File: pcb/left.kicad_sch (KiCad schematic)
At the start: 112 parts, among them J1 PJ-320A, SW1 =, SW10 E, SW11 R, SW12 T, SW13 Esc, SW14 A, SW15 S, SW16 D, SW17 F, SW18 G, SW19 Alt, SW2 1, SW20 Shift, SW21 Z, SW22 X, SW23 C, SW24 V, SW25 B, SW26 Ctrl, SW27 `, SW28 Caps, SW29 Left, SW3 2, SW30 Right, SW31 Super, SW32 Bksp, SW33 Del, SW4 3, SW5 4, SW6 5, SW7 Tab, SW8 Q, SW9 W, SW90 MSK12C02 power, SW91 Reset, U1 nRF52840 Pro Micro

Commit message: Merge both halves into one KiCad project
pcb/keygen.kicad_pro holds a top sheet with left and right sub-sheets
(refs 1xx/2xx, sheet-local nets) and will carry one PCB with both halves
joined by snap-off tabs. The board stays non-reversible. The checker now
runs ERC on the whole project and splits the netlist per half.
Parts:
- removed BT1: LiPo 3.7V ~1000mAh, Connector_JST:JST_PH_S2B-PH-K_1x02_P2.00mm_Horizontal, symbol Device:Battery_Cell
- removed C1: 10uF, Capacitor_SMD:C_0805_2012Metric, symbol Device:C
- removed C2: 100nF, Capacitor_SMD:C_0805_2012Metric, symbol Device:C
- removed D1, D10, D11, D12, D13, D14, D15, D16, D17, D18, D19, D2, D20, D21, D22, D23, D24, D25, D26, D27, D28, D29, D3, D30, D31, D32, D33, D4, D5, D6, D7, D8, D9: 1N4148, Diode_THT:D_DO-35_SOD27_P7.62mm_Horizontal, symbol Device:D
- removed J1: PJ-320A, Keebio-Parts:TRRS-PJ-320A, symbol keygen:TRRS_PJ-320A
- removed LED1, LED10, LED11, LED12, LED13, LED14, LED15, LED16, LED17, LED18, LED19, LED2, LED20, LED21, LED22, LED23, LED24, LED25, LED26, LED27, LED28, LED29, LED3, LED30, LED31, LED32, LED33, LED34, LED35, LED36, LED37, LED38, LED39, LED4, LED5, LED6, LED7, LED8, LED9: SK6812MINI-E, LED_SMD:LED_SK6812MINI-E_3.2x2.8mm_P1.5mm_ReverseMount, symbol LED:SK6812MINI-E
- removed SW1: =, marbastlib-mx:SW_MX_HS_CPG151101S11_1.25u, symbol marbastlib-mx:MX_SW_HS_CPG151101S11
- removed SW10: E, marbastlib-mx:SW_MX_HS_CPG151101S11_1u, symbol marbastlib-mx:MX_SW_HS_CPG151101S11
- removed SW11: R, marbastlib-mx:SW_MX_HS_CPG151101S11_1u, symbol marbastlib-mx:MX_SW_HS_CPG151101S11
- removed SW12: T, marbastlib-mx:SW_MX_HS_CPG151101S11_1u, symbol marbastlib-mx:MX_SW_HS_CPG151101S11
- removed SW13: Esc, marbastlib-mx:SW_MX_HS_CPG151101S11_1.25u, symbol marbastlib-mx:MX_SW_HS_CPG151101S11
- removed SW14: A, marbastlib-mx:SW_MX_HS_CPG151101S11_1u, symbol marbastlib-mx:MX_SW_HS_CPG151101S11
- removed SW15: S, marbastlib-mx:SW_MX_HS_CPG151101S11_1u, symbol marbastlib-mx:MX_SW_HS_CPG151101S11
- removed SW16: D, marbastlib-mx:SW_MX_HS_CPG151101S11_1u, symbol marbastlib-mx:MX_SW_HS_CPG151101S11
- removed SW17: F, marbastlib-mx:SW_MX_HS_CPG151101S11_1u, symbol marbastlib-mx:MX_SW_HS_CPG151101S11
- removed SW18: G, marbastlib-mx:SW_MX_HS_CPG151101S11_1u, symbol marbastlib-mx:MX_SW_HS_CPG151101S11
- removed SW19: Alt, marbastlib-mx:SW_MX_HS_CPG151101S11_1u, symbol marbastlib-mx:MX_SW_HS_CPG151101S11
- removed SW2: 1, marbastlib-mx:SW_MX_HS_CPG151101S11_1u, symbol marbastlib-mx:MX_SW_HS_CPG151101S11
- removed SW20: Shift, marbastlib-mx:SW_MX_HS_CPG151101S11_1.25u, symbol marbastlib-mx:MX_SW_HS_CPG151101S11
- removed SW21: Z, marbastlib-mx:SW_MX_HS_CPG151101S11_1u, symbol marbastlib-mx:MX_SW_HS_CPG151101S11
- removed SW22: X, marbastlib-mx:SW_MX_HS_CPG151101S11_1u, symbol marbastlib-mx:MX_SW_HS_CPG151101S11
- removed SW23: C, marbastlib-mx:SW_MX_HS_CPG151101S11_1u, symbol marbastlib-mx:MX_SW_HS_CPG151101S11
- removed SW24: V, marbastlib-mx:SW_MX_HS_CPG151101S11_1u, symbol marbastlib-mx:MX_SW_HS_CPG151101S11
- removed SW25: B, marbastlib-mx:SW_MX_HS_CPG151101S11_1u, symbol marbastlib-mx:MX_SW_HS_CPG151101S11
- removed SW26: Ctrl, marbastlib-mx:SW_MX_HS_CPG151101S11_1u, symbol marbastlib-mx:MX_SW_HS_CPG151101S11
- removed SW27: `, marbastlib-mx:SW_MX_HS_CPG151101S11_1u, symbol marbastlib-mx:MX_SW_HS_CPG151101S11
- removed SW28: Caps, marbastlib-mx:SW_MX_HS_CPG151101S11_1u, symbol marbastlib-mx:MX_SW_HS_CPG151101S11
- removed SW29: Left, marbastlib-mx:SW_MX_HS_CPG151101S11_1u, symbol marbastlib-mx:MX_SW_HS_CPG151101S11
- removed SW3: 2, marbastlib-mx:SW_MX_HS_CPG151101S11_1u, symbol marbastlib-mx:MX_SW_HS_CPG151101S11
- removed SW30: Right, marbastlib-mx:SW_MX_HS_CPG151101S11_1u, symbol marbastlib-mx:MX_SW_HS_CPG151101S11
- removed SW31: Super, marbastlib-mx:SW_MX_HS_CPG151101S11_1.25u, symbol marbastlib-mx:MX_SW_HS_CPG151101S11
- removed SW32: Bksp, marbastlib-mx:SW_MX_HS_CPG151101S11_1.5u, symbol marbastlib-mx:MX_SW_HS_CPG151101S11
- removed SW33: Del, marbastlib-mx:SW_MX_HS_CPG151101S11_1.5u, symbol marbastlib-mx:MX_SW_HS_CPG151101S11
- removed SW4: 3, marbastlib-mx:SW_MX_HS_CPG151101S11_1u, symbol marbastlib-mx:MX_SW_HS_CPG151101S11
- removed SW5: 4, marbastlib-mx:SW_MX_HS_CPG151101S11_1u, symbol marbastlib-mx:MX_SW_HS_CPG151101S11
- removed SW6: 5, marbastlib-mx:SW_MX_HS_CPG151101S11_1u, symbol marbastlib-mx:MX_SW_HS_CPG151101S11
- removed SW7: Tab, marbastlib-mx:SW_MX_HS_CPG151101S11_1.25u, symbol marbastlib-mx:MX_SW_HS_CPG151101S11
- removed SW8: Q, marbastlib-mx:SW_MX_HS_CPG151101S11_1u, symbol marbastlib-mx:MX_SW_HS_CPG151101S11
- removed SW9: W, marbastlib-mx:SW_MX_HS_CPG151101S11_1u, symbol marbastlib-mx:MX_SW_HS_CPG151101S11
- removed SW90: MSK12C02 power, marbastlib-various:SW_MSK12C02-HB, symbol Switch:SW_SPDT
- removed SW91: Reset, Button_Switch_THT:SW_PUSH_6mm_H5mm, symbol Switch:SW_Push
- removed U1: nRF52840 Pro Micro, marbastlib-xp-promicroish:nice_nano_H_USBup, symbol keygen:nice_nano_v2
- added BT101: LiPo 3.7V ~1000mAh, Connector_JST:JST_PH_S2B-PH-K_1x02_P2.00mm_Horizontal, symbol Device:Battery_Cell
- added C101: 10uF, Capacitor_SMD:C_0805_2012Metric, symbol Device:C
- added C102: 100nF, Capacitor_SMD:C_0805_2012Metric, symbol Device:C
- added D101, D102, D103, D104, D105, D106, D107, D108, D109, D110, D111, D112, D113, D114, D115, D116, D117, D118, D119, D120, D121, D122, D123, D124, D125, D126, D127, D128, D129, D130, D131, D132, D133: 1N4148, Diode_THT:D_DO-35_SOD27_P7.62mm_Horizontal, symbol Device:D
- added J101: PJ-320A, Keebio-Parts:TRRS-PJ-320A, symbol keygen:TRRS_PJ-320A
- added LED101, LED102, LED103, LED104, LED105, LED106, LED107, LED108, LED109, LED110, LED111, LED112, LED113, LED114, LED115, LED116, LED117, LED118, LED119, LED120, LED121, LED122, LED123, LED124, LED125, LED126, LED127, LED128, LED129, LED130, LED131, LED132, LED133, LED134, LED135, LED136, LED137, LED138, LED139: SK6812MINI-E, LED_SMD:LED_SK6812MINI-E_3.2x2.8mm_P1.5mm_ReverseMount, symbol LED:SK6812MINI-E
- added SW101: =, marbastlib-mx:SW_MX_HS_CPG151101S11_1.25u, symbol marbastlib-mx:MX_SW_HS_CPG151101S11
- added SW102: 1, marbastlib-mx:SW_MX_HS_CPG151101S11_1u, symbol marbastlib-mx:MX_SW_HS_CPG151101S11
- added SW103: 2, marbastlib-mx:SW_MX_HS_CPG151101S11_1u, symbol marbastlib-mx:MX_SW_HS_CPG151101S11
- added SW104: 3, marbastlib-mx:SW_MX_HS_CPG151101S11_1u, symbol marbastlib-mx:MX_SW_HS_CPG151101S11
- added SW105: 4, marbastlib-mx:SW_MX_HS_CPG151101S11_1u, symbol marbastlib-mx:MX_SW_HS_CPG151101S11
- added SW106: 5, marbastlib-mx:SW_MX_HS_CPG151101S11_1u, symbol marbastlib-mx:MX_SW_HS_CPG151101S11
- added SW107: Tab, marbastlib-mx:SW_MX_HS_CPG151101S11_1.25u, symbol marbastlib-mx:MX_SW_HS_CPG151101S11
- added SW108: Q, marbastlib-mx:SW_MX_HS_CPG151101S11_1u, symbol marbastlib-mx:MX_SW_HS_CPG151101S11
- added SW109: W, marbastlib-mx:SW_MX_HS_CPG151101S11_1u, symbol marbastlib-mx:MX_SW_HS_CPG151101S11
- added SW110: E, marbastlib-mx:SW_MX_HS_CPG151101S11_1u, symbol marbastlib-mx:MX_SW_HS_CPG151101S11
- added SW111: R, marbastlib-mx:SW_MX_HS_CPG151101S11_1u, symbol marbastlib-mx:MX_SW_HS_CPG151101S11
- added SW112: T, marbastlib-mx:SW_MX_HS_CPG151101S11_1u, symbol marbastlib-mx:MX_SW_HS_CPG151101S11
- added SW113: Esc, marbastlib-mx:SW_MX_HS_CPG151101S11_1.25u, symbol marbastlib-mx:MX_SW_HS_CPG151101S11
- added SW114: A, marbastlib-mx:SW_MX_HS_CPG151101S11_1u, symbol marbastlib-mx:MX_SW_HS_CPG151101S11
- added SW115: S, marbastlib-mx:SW_MX_HS_CPG151101S11_1u, symbol marbastlib-mx:MX_SW_HS_CPG151101S11
- added SW116: D, marbastlib-mx:SW_MX_HS_CPG151101S11_1u, symbol marbastlib-mx:MX_SW_HS_CPG151101S11
- added SW117: F, marbastlib-mx:SW_MX_HS_CPG151101S11_1u, symbol marbastlib-mx:MX_SW_HS_CPG151101S11
- added SW118: G, marbastlib-mx:SW_MX_HS_CPG151101S11_1u, symbol marbastlib-mx:MX_SW_HS_CPG151101S11
- added SW119: Alt, marbastlib-mx:SW_MX_HS_CPG151101S11_1u, symbol marbastlib-mx:MX_SW_HS_CPG151101S11
- added SW120: Shift, marbastlib-mx:SW_MX_HS_CPG151101S11_1.25u, symbol marbastlib-mx:MX_SW_HS_CPG151101S11
- added SW121: Z, marbastlib-mx:SW_MX_HS_CPG151101S11_1u, symbol marbastlib-mx:MX_SW_HS_CPG151101S11
- added SW122: X, marbastlib-mx:SW_MX_HS_CPG151101S11_1u, symbol marbastlib-mx:MX_SW_HS_CPG151101S11
- added SW123: C, marbastlib-mx:SW_MX_HS_CPG151101S11_1u, symbol marbastlib-mx:MX_SW_HS_CPG151101S11
- added SW124: V, marbastlib-mx:SW_MX_HS_CPG151101S11_1u, symbol marbastlib-mx:MX_SW_HS_CPG151101S11
- added SW125: B, marbastlib-mx:SW_MX_HS_CPG151101S11_1u, symbol marbastlib-mx:MX_SW_HS_CPG151101S11
- added SW126: Ctrl, marbastlib-mx:SW_MX_HS_CPG151101S11_1u, symbol marbastlib-mx:MX_SW_HS_CPG151101S11
- added SW127: `, marbastlib-mx:SW_MX_HS_CPG151101S11_1u, symbol marbastlib-mx:MX_SW_HS_CPG151101S11
- added SW128: Caps, marbastlib-mx:SW_MX_HS_CPG151101S11_1u, symbol marbastlib-mx:MX_SW_HS_CPG151101S11
- added SW129: Left, marbastlib-mx:SW_MX_HS_CPG151101S11_1u, symbol marbastlib-mx:MX_SW_HS_CPG151101S11
- added SW130: Right, marbastlib-mx:SW_MX_HS_CPG151101S11_1u, symbol marbastlib-mx:MX_SW_HS_CPG151101S11
- added SW131: Super, marbastlib-mx:SW_MX_HS_CPG151101S11_1.25u, symbol marbastlib-mx:MX_SW_HS_CPG151101S11
- added SW132: Bksp, marbastlib-mx:SW_MX_HS_CPG151101S11_1.5u, symbol marbastlib-mx:MX_SW_HS_CPG151101S11
- added SW133: Del, marbastlib-mx:SW_MX_HS_CPG151101S11_1.5u, symbol marbastlib-mx:MX_SW_HS_CPG151101S11
- added SW190: MSK12C02 power, marbastlib-various:SW_MSK12C02-HB, symbol Switch:SW_SPDT
- added SW191: Reset, Button_Switch_THT:SW_PUSH_6mm_H5mm, symbol Switch:SW_Push
- added U101: nRF52840 Pro Micro, marbastlib-xp-promicroish:nice_nano_H_USBup, symbol keygen:nice_nano_v2
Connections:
- net BAT_RAW: now also BT101.1 (+), SW190.1 (A)
- net COL0: now also SW101.1, SW107.1, SW113.1, SW120.1, SW127.1, U101.12 (P1.06)
- net COL1: now also SW102.1, SW108.1, SW114.1, SW121.1, SW128.1, U101.22 (P1.11)
- net COL2: now also SW103.1, SW109.1, SW115.1, SW122.1, SW129.1, U101.21 (P1.13)
- net COL3: now also SW104.1, SW110.1, SW116.1, SW123.1, SW130.1, U101.20 (P1.15)
- net COL4: now also SW105.1, SW111.1, SW117.1, SW124.1, SW131.1, U101.19 (P0.02)
- net COL5: now also SW106.1, SW112.1, SW118.1, SW125.1, SW132.1, U101.18 (P0.29)
- net COL6: now also SW119.1, SW126.1, SW133.1, U101.17 (P0.31)
- net GND: now also BT101.2 (-), C101.2, C102.2, J101.1 (S), LED101.1 (VSS), LED102.1 (VSS), LED103.1 (VSS), LED104.1 (VSS), LED105.1 (VSS), LED106.1 (VSS), LED107.1 (VSS), LED108.1 (VSS), LED109.1 (VSS), LED110.1 (VSS), LED111.1 (VSS), LED112.1 (VSS), LED113.1 (VSS), LED114.1 (VSS), LED115.1 (VSS), LED116.1 (VSS), LED117.1 (VSS), LED118.1 (VSS), LED119.1 (VSS), LED120.1 (VSS), LED121.1 (VSS), LED122.1 (VSS), LED123.1 (VSS), LED124.1 (VSS), LED125.1 (VSS), LED126.1 (VSS), LED127.1 (VSS), LED128.1 (VSS), LED129.1 (VSS), LED130.1 (VSS), LED131.1 (VSS), LED132.1 (VSS), LED133.1 (VSS), LED134.1 (VSS), LED135.1 (VSS), LED136.1 (VSS), LED137.1 (VSS), LED138.1 (VSS), LED139.1 (VSS), SW191.2, U101.14 (GND), U101.3 (GND), U101.4 (GND)
- net K00: now also D101.2 (A), SW101.2
- net K01: now also D102.2 (A), SW102.2
- net K02: now also D103.2 (A), SW103.2
- net K03: now also D104.2 (A), SW104.2
- net K04: now also D105.2 (A), SW105.2
- net K05: now also D106.2 (A), SW106.2
- net K10: now also D107.2 (A), SW107.2
- net K11: now also D108.2 (A), SW108.2
- net K12: now also D109.2 (A), SW109.2
- net K13: now also D110.2 (A), SW110.2
- net K14: now also D111.2 (A), SW111.2
- net K15: now also D112.2 (A), SW112.2
- net K20: now also D113.2 (A), SW113.2
- net K21: now also D114.2 (A), SW114.2
- net K22: now also D115.2 (A), SW115.2
- net K23: now also D116.2 (A), SW116.2
- net K24: now also D117.2 (A), SW117.2
- net K25: now also D118.2 (A), SW118.2
- net K26: now also D119.2 (A), SW119.2
- net K30: now also D120.2 (A), SW120.2
- net K31: now also D121.2 (A), SW121.2
- net K32: now also D122.2 (A), SW122.2
- net K33: now also D123.2 (A), SW123.2
- net K34: now also D124.2 (A), SW124.2
- net K35: now also D125.2 (A), SW125.2
- net K36: now also D126.2 (A), SW126.2
- net K40: now also D127.2 (A), SW127.2
- net K41: now also D128.2 (A), SW128.2
- net K42: now also D129.2 (A), SW129.2
- net K43: now also D130.2 (A), SW130.2
- net K44: now also D131.2 (A), SW131.2
- net K45: now also D132.2 (A), SW132.2
- net K46: now also D133.2 (A), SW133.2
- net LED_D1: now also LED101.4 (DOUT), LED102.2 (DIN)
- net LED_D10: now also LED110.4 (DOUT), LED111.2 (DIN)
- net LED_D11: now also LED111.4 (DOUT), LED112.2 (DIN)
- net LED_D12: now also LED112.4 (DOUT), LED113.2 (DIN)
- net LED_D13: now also LED113.4 (DOUT), LED114.2 (DIN)
- net LED_D14: now also LED114.4 (DOUT), LED115.2 (DIN)
- net LED_D15: now also LED115.4 (DOUT), LED116.2 (DIN)
- net LED_D16: now also LED116.4 (DOUT), LED117.2 (DIN)
- net LED_D17: now also LED117.4 (DOUT), LED118.2 (DIN)
- net LED_D18: now also LED118.4 (DOUT), LED119.2 (DIN)
- net LED_D19: now also LED119.4 (DOUT), LED120.2 (DIN)
- net LED_D2: now also LED102.4 (DOUT), LED103.2 (DIN)
- net LED_D20: now also LED120.4 (DOUT), LED121.2 (DIN)
- net LED_D21: now also LED121.4 (DOUT), LED122.2 (DIN)
- net LED_D22: now also LED122.4 (DOUT), LED123.2 (DIN)
- net LED_D23: now also LED123.4 (DOUT), LED124.2 (DIN)
- net LED_D24: now also LED124.4 (DOUT), LED125.2 (DIN)
- net LED_D25: now also LED125.4 (DOUT), LED126.2 (DIN)
- net LED_D26: now also LED126.4 (DOUT), LED127.2 (DIN)
- net LED_D27: now also LED127.4 (DOUT), LED128.2 (DIN)
- net LED_D28: now also LED128.4 (DOUT), LED129.2 (DIN)
- net LED_D29: now also LED129.4 (DOUT), LED130.2 (DIN)
- net LED_D3: now also LED103.4 (DOUT), LED104.2 (DIN)
- net LED_D30: now also LED130.4 (DOUT), LED131.2 (DIN)
- net LED_D31: now also LED131.4 (DOUT), LED132.2 (DIN)
- net LED_D32: now also LED132.4 (DOUT), LED133.2 (DIN)
- net LED_D33: now also LED133.4 (DOUT), LED134.2 (DIN)
- net LED_D34: now also LED134.4 (DOUT), LED135.2 (DIN)
- net LED_D35: now also LED135.4 (DOUT), LED136.2 (DIN)
- net LED_D36: now also LED136.4 (DOUT), LED137.2 (DIN)
- net LED_D37: now also LED137.4 (DOUT), LED138.2 (DIN)
- net LED_D38: now also LED138.4 (DOUT), LED139.2 (DIN)
- net LED_D4: now also LED104.4 (DOUT), LED105.2 (DIN)
- net LED_D5: now also LED105.4 (DOUT), LED106.2 (DIN)
- net LED_D6: now also LED106.4 (DOUT), LED107.2 (DIN)
- net LED_D7: now also LED107.4 (DOUT), LED108.2 (DIN)
- net LED_D8: now also LED108.4 (DOUT), LED109.2 (DIN)
- net LED_D9: now also LED109.4 (DOUT), LED110.2 (DIN)
- net LED_DIN: now also LED101.2 (DIN), U101.1 (P0.06)
- net ROW0: now also D101.1 (K), D102.1 (K), D103.1 (K), D104.1 (K), D105.1 (K), D106.1 (K), U101.7 (P0.22)
- net ROW1: now also D107.1 (K), D108.1 (K), D109.1 (K), D110.1 (K), D111.1 (K), D112.1 (K), U101.8 (P0.24)
- net ROW2: now also D113.1 (K), D114.1 (K), D115.1 (K), D116.1 (K), D117.1 (K), D118.1 (K), D119.1 (K), U101.9 (P1.00)
- net ROW3: now also D120.1 (K), D121.1 (K), D122.1 (K), D123.1 (K), D124.1 (K), D125.1 (K), D126.1 (K), U101.10 (P0.11)
- net ROW4: now also D127.1 (K), D128.1 (K), D129.1 (K), D130.1 (K), D131.1 (K), D132.1 (K), D133.1 (K), U101.11 (P1.04)
- net RST: now also SW191.1, U101.15 (RST)
- net UART_RX: now also J101.3 (R1), U101.5 (P0.17)
- net UART_TX: now also J101.2 (T), U101.2 (P0.08)
- net VBAT: now also SW190.2 (B), U101.13 (B+)
- net VCC: now also C101.1, C102.1, LED101.3 (VDD), LED102.3 (VDD), LED103.3 (VDD), LED104.3 (VDD), LED105.3 (VDD), LED106.3 (VDD), LED107.3 (VDD), LED108.3 (VDD), LED109.3 (VDD), LED110.3 (VDD), LED111.3 (VDD), LED112.3 (VDD), LED113.3 (VDD), LED114.3 (VDD), LED115.3 (VDD), LED116.3 (VDD), LED117.3 (VDD), LED118.3 (VDD), LED119.3 (VDD), LED120.3 (VDD), LED121.3 (VDD), LED122.3 (VDD), LED123.3 (VDD), LED124.3 (VDD), LED125.3 (VDD), LED126.3 (VDD), LED127.3 (VDD), LED128.3 (VDD), LED129.3 (VDD), LED130.3 (VDD), LED131.3 (VDD), LED132.3 (VDD), LED133.3 (VDD), LED134.3 (VDD), LED135.3 (VDD), LED136.3 (VDD), LED137.3 (VDD), LED138.3 (VDD), LED139.3 (VDD), U101.16 (VCC)

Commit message: Mark switch bodies on the front silkscreen
pcb/lib/keygen.pretty holds marbastlib's MX hotswap footprints with a
14 mm switch outline on B.SilkS, which lands on the front because the
footprints are placed flipped. Keeping it in a project library (instead
of editing placed footprints) avoids library-mismatch warnings and keeps
'update footprints from library' safe.
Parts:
- SW101, SW107, SW113, SW120, SW131: footprint marbastlib-mx:SW_MX_HS_CPG151101S11_1.25u -> keygen:SW_MX_HS_CPG151101S11_1.25u
- SW102, SW103, SW104, SW105, SW106, SW108, SW109, SW110, SW111, SW112, SW114, SW115, SW116, SW117, SW118, SW119, SW121, SW122, SW123, SW124, SW125, SW126, SW127, SW128, SW129, SW130: footprint marbastlib-mx:SW_MX_HS_CPG151101S11_1u -> keygen:SW_MX_HS_CPG151101S11_1u
- SW132, SW133: footprint marbastlib-mx:SW_MX_HS_CPG151101S11_1.5u -> keygen:SW_MX_HS_CPG151101S11_1.5u

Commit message: Show switches, keycaps and parts in KiCad's 3D view
Project copies of the vendored footprints point their 3D models inside
the repo. The hotswap footprints add a kiswitch MX switch and a generated
keycap, turned over so they stand on the front of a back-mounted part.
The controller gets a simple generated block. The encoder moves to
marbastlib's EC11 footprint (origin at the shaft) because KiCad's
encoder model isn't in the 3D package. Renders in docs/.
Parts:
- J101: footprint Keebio-Parts:TRRS-PJ-320A -> keygen:TRRS-PJ-320A
- SW190: footprint marbastlib-various:SW_MSK12C02-HB -> keygen:SW_MSK12C02-HB
- U101: footprint marbastlib-xp-promicroish:nice_nano_H_USBup -> keygen:nice_nano_H_USBup

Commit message: Route the PCB: DRC clean with schematic parity
Freerouting routes ~85% of signals with ground left to the pour; a grid
maze router (finish_route.py) completes the rest and ties stranded
ground pads to vias. Ground is poured on both layers per half with
stitching vias, islands removed and an antenna keep-out under each
controller. sync_pcb.py relinks footprints to the schematic; schematic
UUIDs are now deterministic so regenerating keeps those links, and the
generator no longer overwrites the project's design rules. Mounting
holes are in the schematic. Result: 0 unconnected, 0 errors, 0 parity
issues (28 silkscreen warnings remain).
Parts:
- added H101, H102, H103, H104, H105: M2, MountingHole:MountingHole_2.2mm_M2, symbol Mechanical:MountingHole
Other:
- note added: "MOUNTING HOLES (M2)"

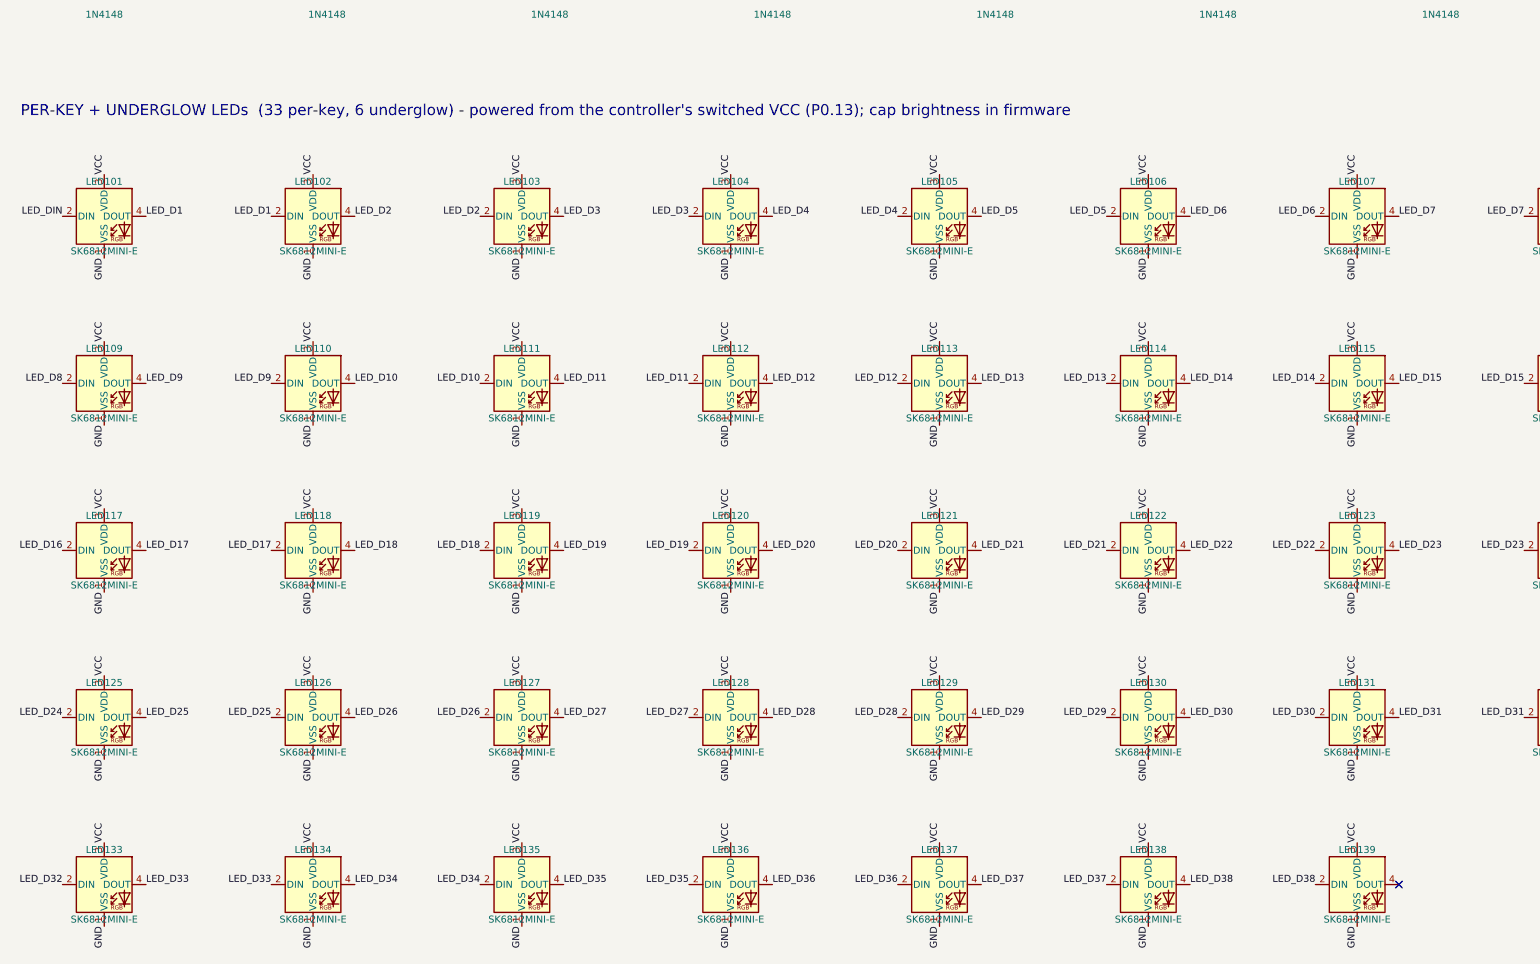
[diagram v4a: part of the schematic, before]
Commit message: Drop the underglow LEDs
The battery sits under the PCB, where it would hide the six underglow
LEDs per half and they would only drain it. The LED chain is now the 33
per-key LEDs on each half (LED x01-x33), all reverse-mounted on the back.

The schematic and placement generators no longer add them. On the routed
board the 12 footprints and their chain copper were removed, the VCC
links they carried were re-routed with finish_route.py, and DRC with
schematic parity is clean (0 errors, 0 unconnected). Gerbers, BOMs, the
schematic PDF, the plan and the shopping list are regenerated.

(Cherry-picked from 8c0cb53, made on the board before the tracks were
straightened; the board surgery, VCC re-route and outputs were redone
on the straightened board.)
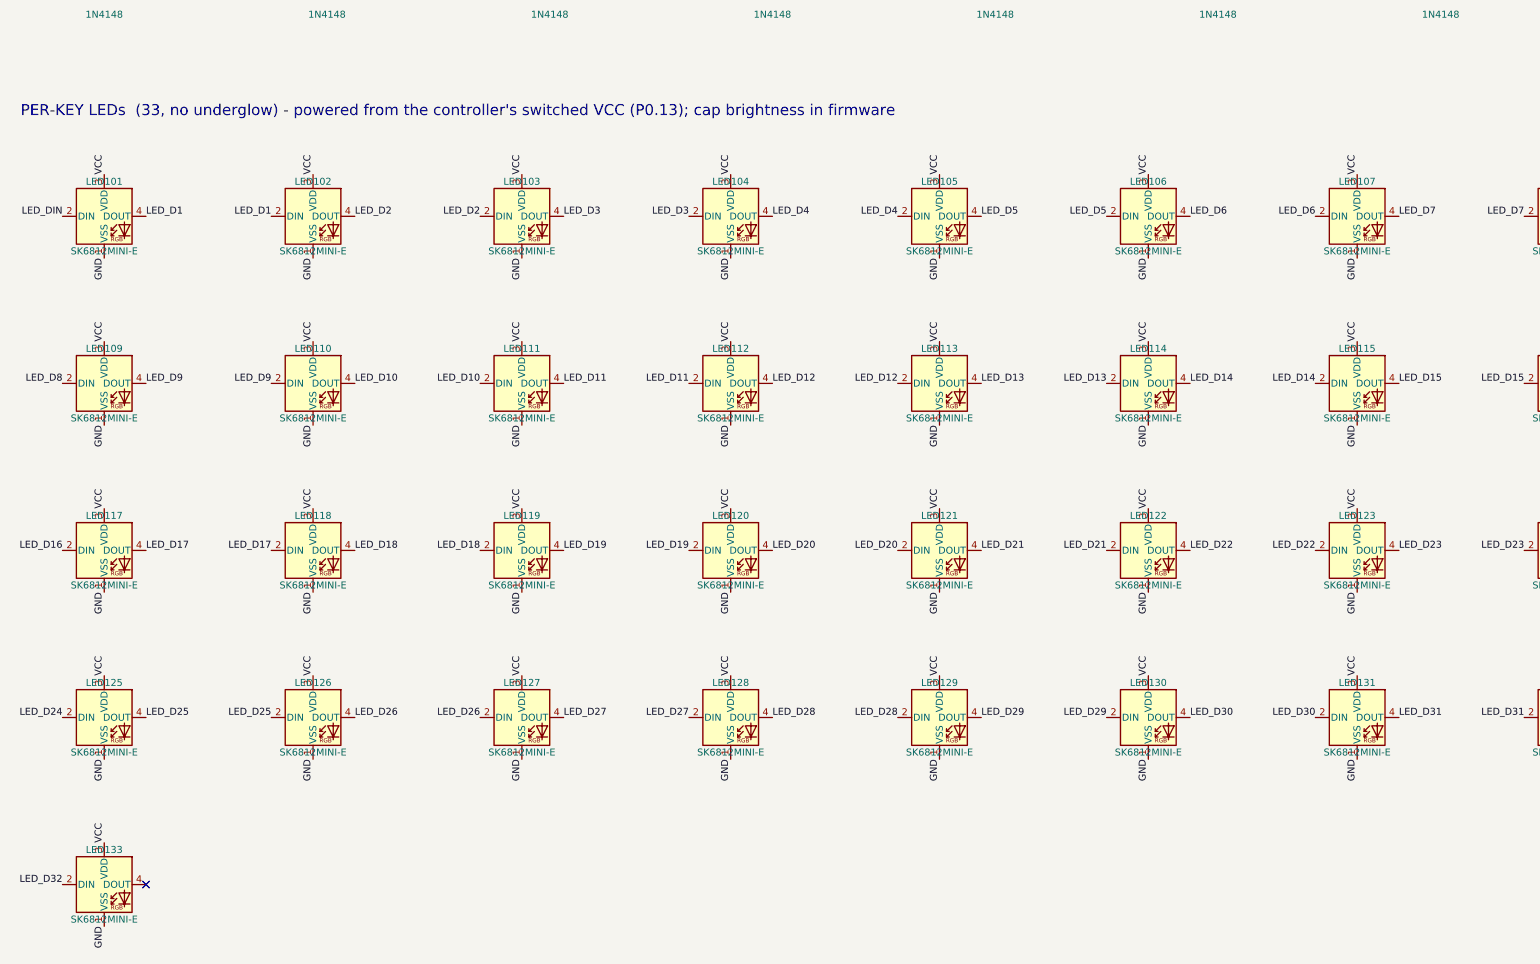
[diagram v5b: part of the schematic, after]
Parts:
- removed LED134, LED135, LED136, LED137, LED138, LED139: SK6812MINI-E, LED_SMD:LED_SK6812MINI-E_3.2x2.8mm_P1.5mm_ReverseMount, symbol LED:SK6812MINI-E
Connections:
- net LED_D33: no longer names the net of LED133.4 (DOUT)
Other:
- note added: "PER-KEY LEDs (33, no underglow) - powered from the controller's switched VCC (P0.13); cap brightness in firmware"
- note removed: "PER-KEY + UNDERGLOW LEDs (33 per-key, 6 underglow) - powered from the controller's switched VCC (P0.13); cap brightness in firmware"
